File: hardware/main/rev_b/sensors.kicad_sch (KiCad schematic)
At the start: 16 parts, among them U20 ICM-42688-P, U21 LSM6DSO32TR, U22 LPS22DFTR

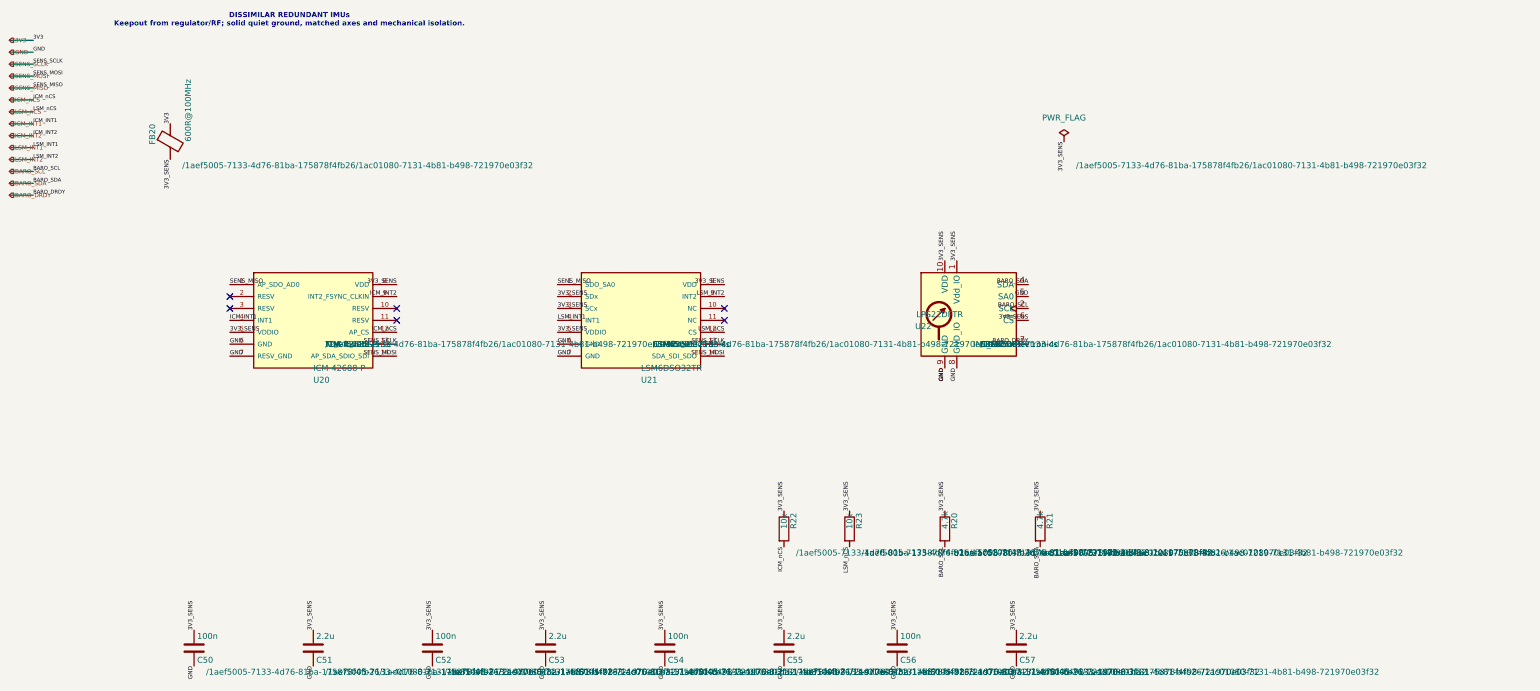
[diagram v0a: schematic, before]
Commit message: fix: consolidate portable Rev-B hardware sources
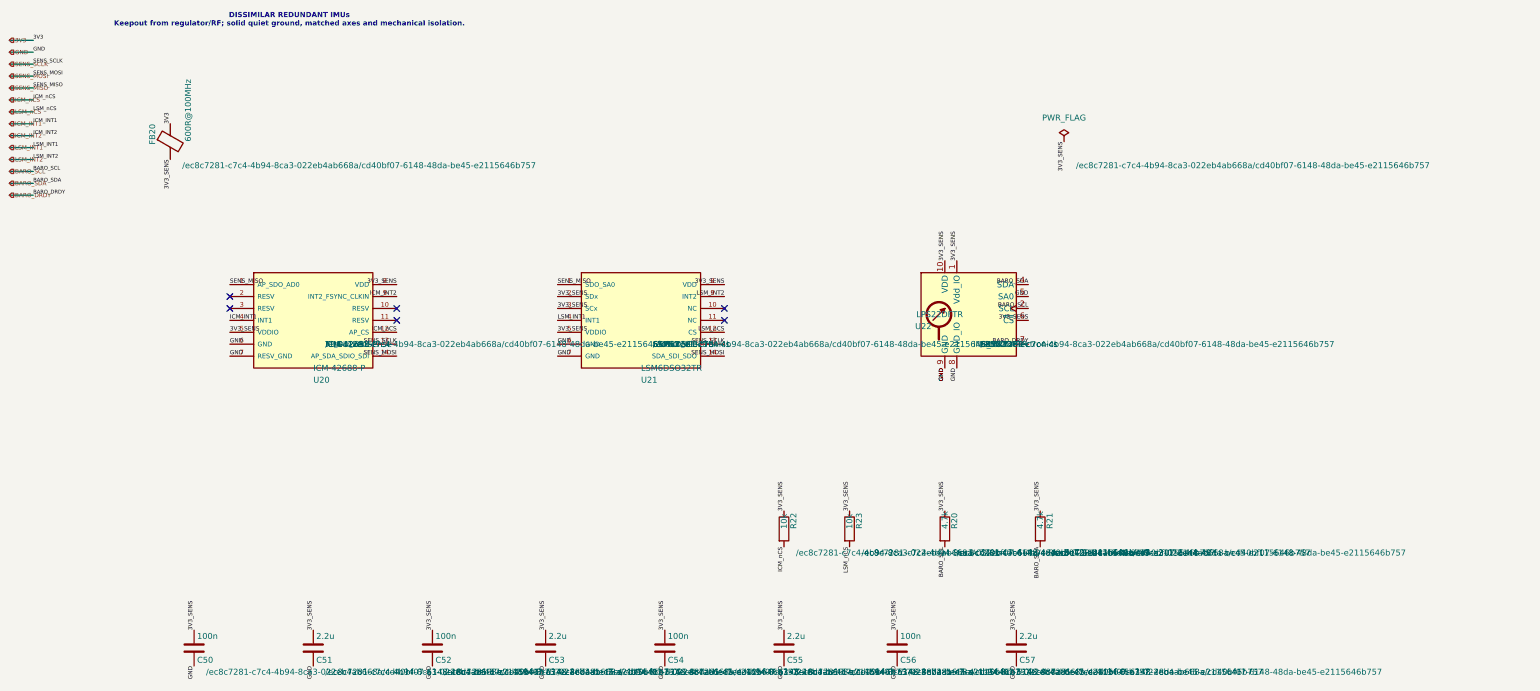
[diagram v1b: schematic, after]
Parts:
- C50, C51, C52, C53, C54, C55, C56, C57, FB20, R20, R21, R22, R23, U20, U21, U22: hierarchy_path /1aef5005-7133-4d76-81ba-175878f4fb26/1ac01080-7131-4b81-b4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 -> /ec8c7281-c7c4-4b94-8ca3-022eb4ab668a/cd40bf07-6148-48da-be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
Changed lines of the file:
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@@
 			)
 		)
-		(property "hierarchy_path" "/1aef5005-7133-4d76-81ba-175878f4fb26/1ac01080-7131-4b81-b498-721970e03f32"
+		(property "hierarchy_path" "/ec8c7281-c7c4-4b94-8ca3-022eb4ab668a/cd40bf07-6148-48da-be45-e2115646b757"
 			(at 57.15 46.9899 0)
 			(effects
@@
 		(instances
 			(project "main_rev_b"
-				(path "/1aef5005-7133-4d76-81ba-175878f4fb26/1ac01080-7131-4b81-b498-721970e03f32"
+				(path "/ec8c7281-c7c4-4b94-8ca3-022eb4ab668a/cd40bf07-6148-48da-be45-e2115646b757"
 					(reference "FB20")
 					(unit 1)
@@
 			)
 		)
-		(property "hierarchy_path" "/1aef5005-7133-4d76-81ba-175878f4fb26/1ac01080-7131-4b81-b498-721970e03f32"
+		(property "hierarchy_path" "/ec8c7281-c7c4-4b94-8ca3-022eb4ab668a/cd40bf07-6148-48da-be45-e2115646b757"
 			(at 87.63 85.0899 0)
 			(effects
@@
 		(instances
 			(project "main_rev_b"
-				(path "/1aef5005-7133-4d76-81ba-175878f4fb26/1ac01080-7131-4b81-b498-721970e03f32"
+				(path "/ec8c7281-c7c4-4b94-8ca3-022eb4ab668a/cd40bf07-6148-48da-be45-e2115646b757"
 					(reference "U20")
 					(unit 1)
@@
 			)
 		)
-		(property "hierarchy_path" "/1aef5005-7133-4d76-81ba-175878f4fb26/1ac01080-7131-4b81-b498-721970e03f32"
+		(property "hierarchy_path" "/ec8c7281-c7c4-4b94-8ca3-022eb4ab668a/cd40bf07-6148-48da-be45-e2115646b757"
 			(at 157.48 85.0899 0)
 			(effects
@@
 		(instances
 			(project "main_rev_b"
-				(path "/1aef5005-7133-4d76-81ba-175878f4fb26/1ac01080-7131-4b81-b498-721970e03f32"
+				(path "/ec8c7281-c7c4-4b94-8ca3-022eb4ab668a/cd40bf07-6148-48da-be45-e2115646b757"
 					(reference "U21")
 					(unit 1)
@@
 			)
 		)
-		(property "hierarchy_path" "/1aef5005-7133-4d76-81ba-175878f4fb26/1ac01080-7131-4b81-b498-721970e03f32"
+		(property "hierarchy_path" "/ec8c7281-c7c4-4b94-8ca3-022eb4ab668a/cd40bf07-6148-48da-be45-e2115646b757"
 			(at 227.33 85.0899 0)
 			(effects
@@
 		(instances
 			(project "main_rev_b"
-				(path "/1aef5005-7133-4d76-81ba-175878f4fb26/1ac01080-7131-4b81-b498-721970e03f32"
+				(path "/ec8c7281-c7c4-4b94-8ca3-022eb4ab668a/cd40bf07-6148-48da-be45-e2115646b757"
 					(reference "U22")
 					(unit 1)
@@
 			)
 		)
-		(property "hierarchy_path" "/1aef5005-7133-4d76-81ba-175878f4fb26/1ac01080-7131-4b81-b498-721970e03f32"
+		(property "hierarchy_path" "/ec8c7281-c7c4-4b94-8ca3-022eb4ab668a/cd40bf07-6148-48da-be45-e2115646b757"
 			(at 222.25 129.5399 0)
 			(effects
@@
 		(instances
 			(project "main_rev_b"
-				(path "/1aef5005-7133-4d76-81ba-175878f4fb26/1ac01080-7131-4b81-b498-721970e03f32"
+				(path "/ec8c7281-c7c4-4b94-8ca3-022eb4ab668a/cd40bf07-6148-48da-be45-e2115646b757"
 					(reference "R20")
 					(unit 1)
@@
 			)
 		)
-		(property "hierarchy_path" "/1aef5005-7133-4d76-81ba-175878f4fb26/1ac01080-7131-4b81-b498-721970e03f32"
+		(property "hierarchy_path" "/ec8c7281-c7c4-4b94-8ca3-022eb4ab668a/cd40bf07-6148-48da-be45-e2115646b757"
 			(at 242.57 129.5399 0)
 			(effects
@@
 		(instances
 			(project "main_rev_b"
-				(path "/1aef5005-7133-4d76-81ba-175878f4fb26/1ac01080-7131-4b81-b498-721970e03f32"
+				(path "/ec8c7281-c7c4-4b94-8ca3-022eb4ab668a/cd40bf07-6148-48da-be45-e2115646b757"
 					(reference "R21")
 					(unit 1)
@@
 			)
 		)
-		(property "hierarchy_path" "/1aef5005-7133-4d76-81ba-175878f4fb26/1ac01080-7131-4b81-b498-721970e03f32"
+		(property "hierarchy_path" "/ec8c7281-c7c4-4b94-8ca3-022eb4ab668a/cd40bf07-6148-48da-be45-e2115646b757"
 			(at 187.96 129.5399 0)
 			(effects
@@
 		(instances
 			(project "main_rev_b"
-				(path "/1aef5005-7133-4d76-81ba-175878f4fb26/1ac01080-7131-4b81-b498-721970e03f32"
+				(path "/ec8c7281-c7c4-4b94-8ca3-022eb4ab668a/cd40bf07-6148-48da-be45-e2115646b757"
 					(reference "R22")
 					(unit 1)
@@
 			)
 		)
-		(property "hierarchy_path" "/1aef5005-7133-4d76-81ba-175878f4fb26/1ac01080-7131-4b81-b498-721970e03f32"
+		(property "hierarchy_path" "/ec8c7281-c7c4-4b94-8ca3-022eb4ab668a/cd40bf07-6148-48da-be45-e2115646b757"
 			(at 201.93 129.5399 0)
 			(effects
@@
 		(instances
 			(project "main_rev_b"
-				(path "/1aef5005-7133-4d76-81ba-175878f4fb26/1ac01080-7131-4b81-b498-721970e03f32"
+				(path "/ec8c7281-c7c4-4b94-8ca3-022eb4ab668a/cd40bf07-6148-48da-be45-e2115646b757"
 					(reference "R23")
 					(unit 1)
@@
 			)
 		)
-		(property "hierarchy_path" "/1aef5005-7133-4d76-81ba-175878f4fb26/1ac01080-7131-4b81-b498-721970e03f32"
+		(property "hierarchy_path" "/ec8c7281-c7c4-4b94-8ca3-022eb4ab668a/cd40bf07-6148-48da-be45-e2115646b757"
 			(at 62.23 154.9399 0)
 			(effects
@@
 		(instances
 			(project "main_rev_b"
-				(path "/1aef5005-7133-4d76-81ba-175878f4fb26/1ac01080-7131-4b81-b498-721970e03f32"
+				(path "/ec8c7281-c7c4-4b94-8ca3-022eb4ab668a/cd40bf07-6148-48da-be45-e2115646b757"
 					(reference "C50")
 					(unit 1)
@@
 			)
 		)
-		(property "hierarchy_path" "/1aef5005-7133-4d76-81ba-175878f4fb26/1ac01080-7131-4b81-b498-721970e03f32"
+		(property "hierarchy_path" "/ec8c7281-c7c4-4b94-8ca3-022eb4ab668a/cd40bf07-6148-48da-be45-e2115646b757"
 			(at 87.63 154.9399 0)
 			(effects
@@
 		(instances
 			(project "main_rev_b"
-				(path "/1aef5005-7133-4d76-81ba-175878f4fb26/1ac01080-7131-4b81-b498-721970e03f32"
+				(path "/ec8c7281-c7c4-4b94-8ca3-022eb4ab668a/cd40bf07-6148-48da-be45-e2115646b757"
 					(reference "C51")
 					(unit 1)
@@
 			)
 		)
-		(property "hierarchy_path" "/1aef5005-7133-4d76-81ba-175878f4fb26/1ac01080-7131-4b81-b498-721970e03f32"
+		(property "hierarchy_path" "/ec8c7281-c7c4-4b94-8ca3-022eb4ab668a/cd40bf07-6148-48da-be45-e2115646b757"
 			(at 113.03 154.9399 0)
 			(effects
@@
 		(instances
 			(project "main_rev_b"
-				(path "/1aef5005-7133-4d76-81ba-175878f4fb26/1ac01080-7131-4b81-b498-721970e03f32"
+				(path "/ec8c7281-c7c4-4b94-8ca3-022eb4ab668a/cd40bf07-6148-48da-be45-e2115646b757"
 					(reference "C52")
 					(unit 1)
@@
 			)
 		)
-		(property "hierarchy_path" "/1aef5005-7133-4d76-81ba-175878f4fb26/1ac01080-7131-4b81-b498-721970e03f32"
+		(property "hierarchy_path" "/ec8c7281-c7c4-4b94-8ca3-022eb4ab668a/cd40bf07-6148-48da-be45-e2115646b757"
 			(at 137.16 154.9399 0)
 			(effects
@@
 		(instances
 			(project "main_rev_b"
-				(path "/1aef5005-7133-4d76-81ba-175878f4fb26/1ac01080-7131-4b81-b498-721970e03f32"
+				(path "/ec8c7281-c7c4-4b94-8ca3-022eb4ab668a/cd40bf07-6148-48da-be45-e2115646b757"
 					(reference "C53")
 					(unit 1)
@@
 			)
 		)
-		(property "hierarchy_path" "/1aef5005-7133-4d76-81ba-175878f4fb26/1ac01080-7131-4b81-b498-721970e03f32"
+		(property "hierarchy_path" "/ec8c7281-c7c4-4b94-8ca3-022eb4ab668a/cd40bf07-6148-48da-be45-e2115646b757"
 			(at 162.56 154.9399 0)
 			(effects
@@
 		(instances
 			(project "main_rev_b"
-				(path "/1aef5005-7133-4d76-81ba-175878f4fb26/1ac01080-7131-4b81-b498-721970e03f32"
+				(path "/ec8c7281-c7c4-4b94-8ca3-022eb4ab668a/cd40bf07-6148-48da-be45-e2115646b757"
 					(reference "C54")
 					(unit 1)
@@
 			)
 		)
-		(property "hierarchy_path" "/1aef5005-7133-4d76-81ba-175878f4fb26/1ac01080-7131-4b81-b498-721970e03f32"
+		(property "hierarchy_path" "/ec8c7281-c7c4-4b94-8ca3-022eb4ab668a/cd40bf07-6148-48da-be45-e2115646b757"
 			(at 187.96 154.9399 0)
 			(effects
@@
 		(instances
 			(project "main_rev_b"
-				(path "/1aef5005-7133-4d76-81ba-175878f4fb26/1ac01080-7131-4b81-b498-721970e03f32"
+				(path "/ec8c7281-c7c4-4b94-8ca3-022eb4ab668a/cd40bf07-6148-48da-be45-e2115646b757"
 					(reference "C55")
 					(unit 1)
@@
 			)
 		)
-		(property "hierarchy_path" "/1aef5005-7133-4d76-81ba-175878f4fb26/1ac01080-7131-4b81-b498-721970e03f32"
+		(property "hierarchy_path" "/ec8c7281-c7c4-4b94-8ca3-022eb4ab668a/cd40bf07-6148-48da-be45-e2115646b757"
 			(at 212.09 154.9399 0)
 			(effects
@@
 		(instances
 			(project "main_rev_b"
-				(path "/1aef5005-7133-4d76-81ba-175878f4fb26/1ac01080-7131-4b81-b498-721970e03f32"
+				(path "/ec8c7281-c7c4-4b94-8ca3-022eb4ab668a/cd40bf07-6148-48da-be45-e2115646b757"
 					(reference "C56")
 					(unit 1)
@@
 			)
 		)
-		(property "hierarchy_path" "/1aef5005-7133-4d76-81ba-175878f4fb26/1ac01080-7131-4b81-b498-721970e03f32"
+		(property "hierarchy_path" "/ec8c7281-c7c4-4b94-8ca3-022eb4ab668a/cd40bf07-6148-48da-be45-e2115646b757"
 			(at 237.49 154.9399 0)
 			(effects
@@
 		(instances
 			(project "main_rev_b"
-				(path "/1aef5005-7133-4d76-81ba-175878f4fb26/1ac01080-7131-4b81-b498-721970e03f32"
+				(path "/ec8c7281-c7c4-4b94-8ca3-022eb4ab668a/cd40bf07-6148-48da-be45-e2115646b757"
 					(reference "C57")
 					(unit 1)
@@
 			)
 		)
-		(property "hierarchy_path" "/1aef5005-7133-4d76-81ba-175878f4fb26/1ac01080-7131-4b81-b498-721970e03f32"
+		(property "hierarchy_path" "/ec8c7281-c7c4-4b94-8ca3-022eb4ab668a/cd40bf07-6148-48da-be45-e2115646b757"
 			(at 247.65 46.9899 0)
 			(effects
@@
 		(instances
 			(project "main_rev_b"
-				(path "/1aef5005-7133-4d76-81ba-175878f4fb26/1ac01080-7131-4b81-b498-721970e03f32"
+				(path "/ec8c7281-c7c4-4b94-8ca3-022eb4ab668a/cd40bf07-6148-48da-be45-e2115646b757"
 					(reference "#FLG20")
 					(unit 1)
